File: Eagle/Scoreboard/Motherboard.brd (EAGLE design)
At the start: 59.4 x 80 mm, 24 parts

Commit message: Changed transistor type for score controller, changed number of terminals to 8. Motherboard still TBD
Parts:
- removed DISP_POWER: (no value), con-wago-500:W237-102
- added 12V, LED: (no value), con-wago-500:W237-102
- added R7: 470, resistor:0204/5
- added SG1: EB2505, buzzer:EB2505
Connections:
- new net 12V: 12V.1, 12V.2, C1.+, R7.2, REG.1, VCC.1
- net GND: now also LED.1; no longer DISP_POWER.1
- net N$7: now also LED.2, R7.1; no longer C1.+, REG.1, VCC.1
- net VCC: no longer DISP_POWER.2
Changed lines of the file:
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@@
 <attribute name="SPICEPREFIX" value="C" x="45.72" y="64.77" size="1.778" layer="27" rot="R270" display="off"/>
-</element>
-<element name="DISP_POWER" library="con-wago-500" library_urn="urn:adsk.eagle:library:195" package="W237-102" package3d_urn="urn:adsk.eagle:package:10688/1" value="" x="53.34" y="55.88" rot="R90">
-<attribute name="MF" value="" x="53.34" y="55.88" size="1.778" layer="27" rot="R90" display="off"/>
-<attribute name="MPN" value="237-102" x="53.34" y="55.88" size="1.778" layer="27" rot="R90" display="off"/>
-<attribute name="OC_FARNELL" value="unknown" x="53.34" y="55.88" size="1.778" layer="27" rot="R90" display="off"/>
-<attribute name="OC_NEWARK" value="70K9898" x="53.34" y="55.88" size="1.778" layer="27" rot="R90" display="off"/>
 </element>
 <element name="INFRA" library="con-wago-500" library_urn="urn:adsk.eagle:library:195" package="W237-103" package3d_urn="urn:adsk.eagle:package:10691/1" value="" x="53.34" y="12.7" rot="R90">
@@
 </element>
 <element name="R6" library="resistor" library_urn="urn:adsk.eagle:library:348" package="0204/5" package3d_urn="urn:adsk.eagle:package:25955/1" value="10k" x="30.48" y="15.24" rot="R180"/>
+<element name="12V" library="con-wago-500" library_urn="urn:adsk.eagle:library:195" package="W237-102" package3d_urn="urn:adsk.eagle:package:10688/1" value="" x="-7.62" y="8.89">
+<attribute name="MF" value="" x="-7.62" y="8.89" size="1.778" layer="27" display="off"/>
+<attribute name="MPN" value="237-102" x="-7.62" y="8.89" size="1.778" layer="27" display="off"/>
+<attribute name="OC_FARNELL" value="unknown" x="-7.62" y="8.89" size="1.778" layer="27" display="off"/>
+<attribute name="OC_NEWARK" value="70K9898" x="-7.62" y="8.89" size="1.778" layer="27" display="off"/>
+</element>
+<element name="R7" library="resistor" library_urn="urn:adsk.eagle:library:348" package="0204/5" package3d_urn="urn:adsk.eagle:package:25955/1" value="470" x="-8.89" y="-3.81"/>
+<element name="LED" library="con-wago-500" library_urn="urn:adsk.eagle:library:195" package="W237-102" package3d_urn="urn:adsk.eagle:package:10688/1" value="" x="-17.78" y="2.54">
+<attribute name="MF" value="" x="-17.78" y="2.54" size="1.778" layer="27" display="off"/>
+<attribute name="MPN" value="237-102" x="-17.78" y="2.54" size="1.778" layer="27" display="off"/>
+<attribute name="OC_FARNELL" value="unknown" x="-17.78" y="2.54" size="1.778" layer="27" display="off"/>
+<attribute name="OC_NEWARK" value="70K9898" x="-17.78" y="2.54" size="1.778" layer="27" display="off"/>
+</element>
+<element name="SG1" library="buzzer" library_urn="urn:adsk.eagle:library:113" package="EB2505" package3d_urn="urn:adsk.eagle:package:5275/1" value="EB2505" x="-35.56" y="6.35">
+<attribute name="MF" value="" x="-35.56" y="6.35" size="1.778" layer="27" display="off"/>
+<attribute name="MPN" value="" x="-35.56" y="6.35" size="1.778" layer="27" display="off"/>
+<attribute name="OC_FARNELL" value="unknown" x="-35.56" y="6.35" size="1.778" layer="27" display="off"/>
+<attribute name="OC_NEWARK" value="unknown" x="-35.56" y="6.35" size="1.778" layer="27" display="off"/>
+</element>
 </elements>
 <signals>
@@
 <contactref element="BTN_POW" pad="2"/>
 <contactref element="BLUETOOTH1" pad="2"/>
-<contactref element="DISP_POWER" pad="1"/>
 <contactref element="INFRA" pad="2"/>
 <contactref element="433MHZ" pad="1"/>
 <contactref element="ARDUINO_NANO1" pad="18"/>
 <contactref element="R6" pad="2"/>
+<contactref element="LED" pad="1"/>
 <wire x1="45.72" y1="63.754" x2="54.61" y2="68.54" width="0" layer="19" extent="1-1"/>
 <wire x1="39.37" y1="63.5" x2="45.72" y2="63.754" width="0" layer="19" extent="1-1"/>
@@
 <wire x1="40.68" y1="76.2" x2="35.56" y2="75.184" width="0" layer="19" extent="1-1"/>
 <wire x1="24.17" y1="76.2" x2="35.56" y2="75.184" width="0" layer="19" extent="1-1"/>
-<wire x1="54.61" y1="53.38" x2="45.72" y2="63.754" width="0" layer="19" extent="1-1"/>
-<wire x1="35.56" y1="35.56" x2="54.61" y2="53.38" width="0" layer="19" extent="1-1"/>
+<wire x1="35.56" y1="35.56" x2="39.37" y2="63.5" width="0" layer="19" extent="1-1"/>
 <wire x1="33.02" y1="35.56" x2="35.56" y2="35.56" width="0" layer="19" extent="1-1"/>
 <wire x1="38.1" y1="20.32" x2="35.56" y2="35.56" width="0" layer="19" extent="1-1"/>
@@
 <wire x1="54.63" y1="22.94" x2="38.1" y2="20.32" width="0" layer="19" extent="1-1"/>
 <wire x1="54.63" y1="12.7" x2="54.63" y2="22.94" width="0" layer="19" extent="1-1"/>
+<wire x1="-20.28" y1="1.27" x2="13.97" y2="12.7" width="0" layer="19" extent="1-1"/>
 </signal>
 <signal name="N$1">
@@
 <wire x1="34.25" y1="5.08" x2="27.94" y2="12.7" width="0" layer="19" extent="1-1"/>
 </signal>
-<signal name="N$7">
+<signal name="12V">
 <contactref element="VCC" pad="1"/>
 <contactref element="REG" pad="1"/>
 <contactref element="C1" pad="+"/>
+<contactref element="12V" pad="1"/>
+<contactref element="12V" pad="2"/>
+<contactref element="R7" pad="2"/>
 <wire x1="29.17" y1="76.2" x2="35.56" y2="77.216" width="0" layer="19" extent="1-1"/>
 <wire x1="39.37" y1="60.96" x2="35.56" y2="77.216" width="0" layer="19" extent="1-1"/>
+<wire x1="-5.12" y1="7.62" x2="39.37" y2="60.96" width="0" layer="19" extent="1-1"/>
+<wire x1="-10.12" y1="7.62" x2="-5.12" y2="7.62" width="0" layer="19" extent="1-1"/>
+<wire x1="-6.35" y1="-3.81" x2="-5.12" y2="7.62" width="0" layer="19" extent="1-1"/>
 </signal>
 <signal name="N$8">
@@
 <contactref element="BTN_POW" pad="1"/>
 <contactref element="BLUETOOTH1" pad="1"/>
-<contactref element="DISP_POWER" pad="2"/>
 <contactref element="INFRA" pad="3"/>
 <contactref element="433MHZ" pad="2"/>
 <wire x1="54.61" y1="63.54" x2="45.68" y2="76.2" width="0" layer="19" extent="1-1"/>
-<wire x1="54.61" y1="58.38" x2="54.61" y2="63.54" width="0" layer="19" extent="1-1"/>
-<wire x1="54.63" y1="27.94" x2="54.61" y2="58.38" width="0" layer="19" extent="1-1"/>
+<wire x1="54.63" y1="27.94" x2="54.61" y2="63.54" width="0" layer="19" extent="1-1"/>
 <wire x1="54.63" y1="17.7" x2="54.63" y2="27.94" width="0" layer="19" extent="1-1"/>
 <wire x1="33.02" y1="20.32" x2="54.63" y2="17.7" width="0" layer="19" extent="1-1"/>
@@
 <wire x1="5.08" y1="20.32" x2="54.63" y2="48.18" width="0" layer="19" extent="1-1"/>
 </signal>
+<signal name="N$7">
+<contactref element="R7" pad="1"/>
+<contactref element="LED" pad="2"/>
+<wire x1="-11.43" y1="-3.81" x2="-15.28" y2="1.27" width="0" layer="19" extent="1-1"/>
+</signal>
 </signals>

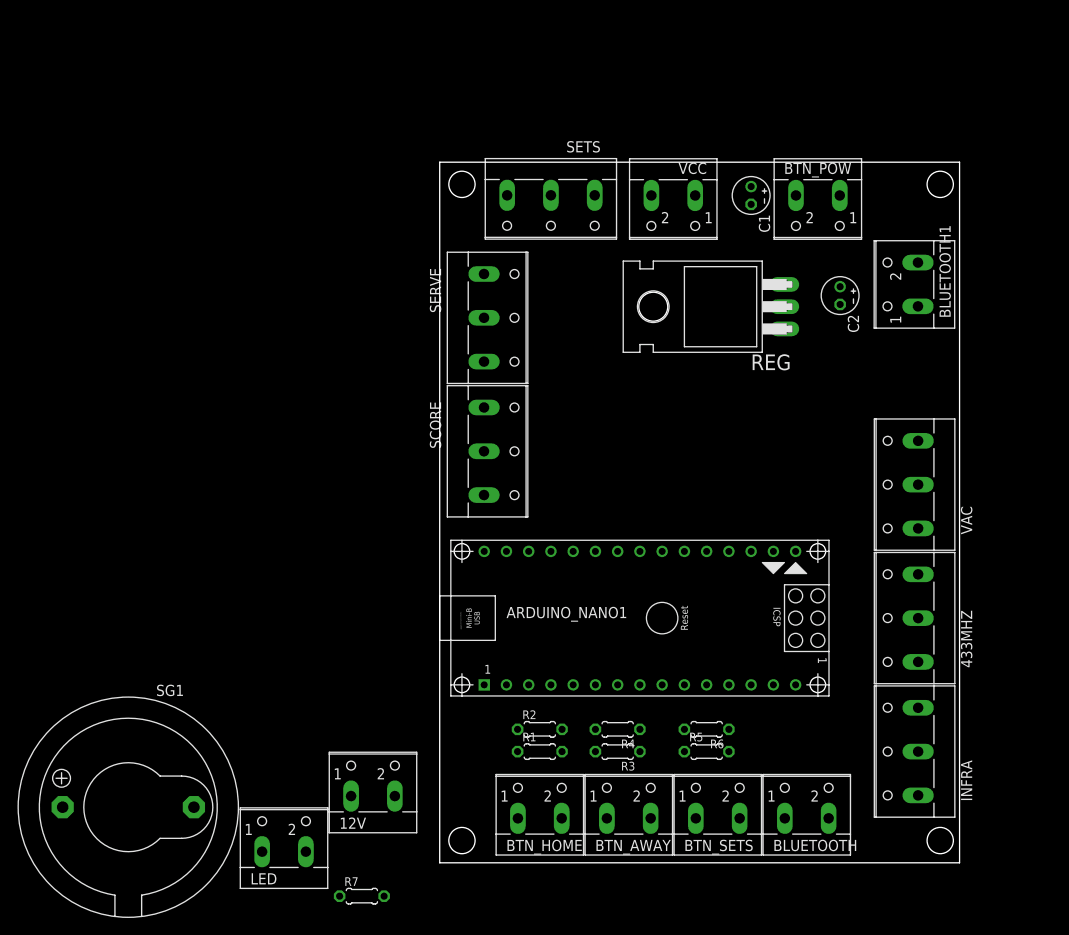
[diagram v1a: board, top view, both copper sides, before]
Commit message: Changed matherboard scheme and start designing PCB
Scheme was changed to make easier PCB design. Still need to finish VCC layer on TOP layer
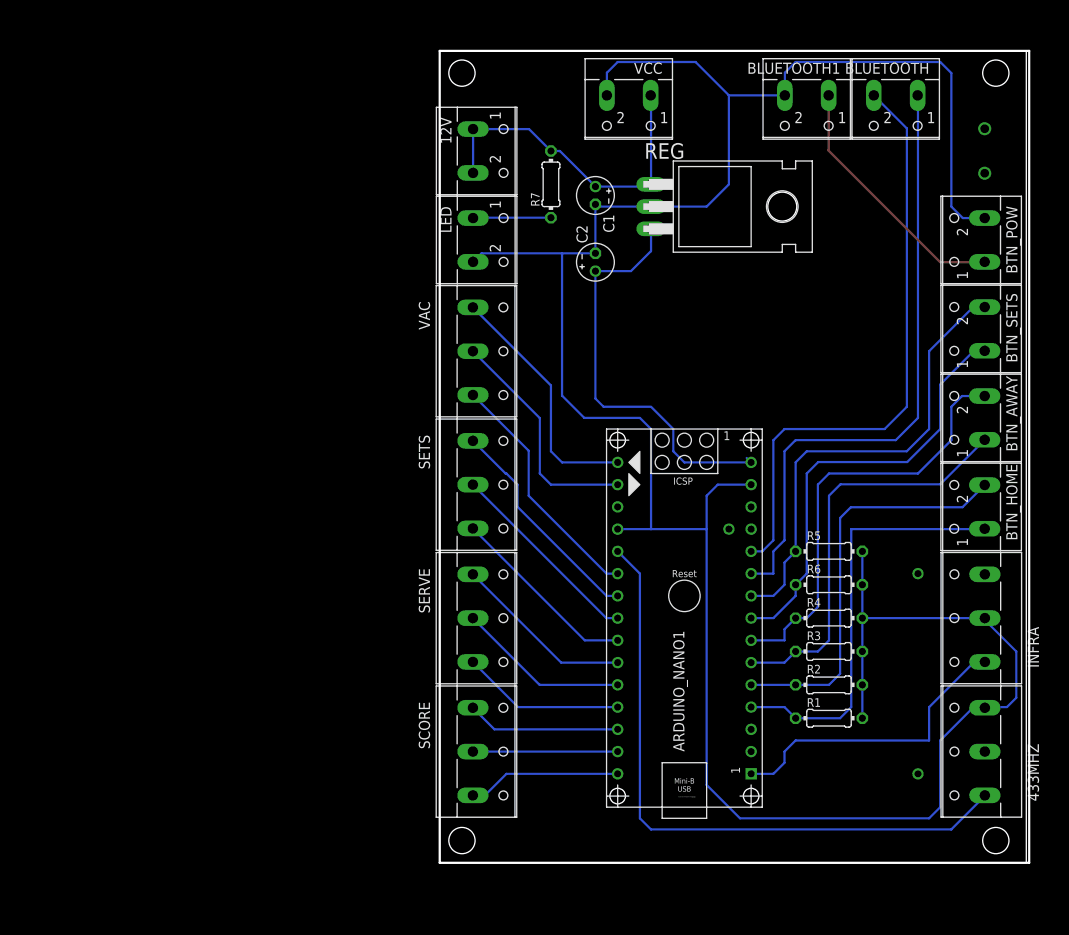
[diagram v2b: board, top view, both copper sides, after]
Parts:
- removed SG1: EB2505, buzzer:EB2505
- R1, R2, R3, R4, R5, R6, R7: device resistor:0204/5 -> resistor:0204/7
- moved R7 84.1 mm to (12.7, 77.5), turned to 90 degrees
- moved BLUETOOTH 80.7 mm to (52.1, 86.4), turned to 180 degrees
- moved 12V 73.5 mm to (5.08, 81.3), turned to 270 degrees
- moved LED 72.3 mm to (5.08, 71.1), turned to 270 degrees
- moved BTN_SETS 61.9 mm to (61.0, 61.0), turned to 90 degrees
- moved BTN_HOME 60.2 mm to (61.0, 40.6), turned to 90 degrees
- moved BTN_AWAY 59.4 mm to (61.0, 50.8), turned to 90 degrees
- moved VAC 50.6 mm to (5.08, 58.4), turned to 270 degrees
- moved SCORE 34.3 mm to (5.08, 12.7)
- moved SERVE 34.3 mm to (5.08, 27.9)
- moved R2 33.4 mm to (44.5, 20.3)
- moved R1 33.2 mm to (44.5, 16.5)
- moved SETS 32.7 mm to (5.08, 43.2), turned to 270 degrees
- moved C2 28.2 mm to (17.8, 68.6), turned to 90 degrees
- moved R4 27.3 mm to (44.5, 27.9), turned to 0 degrees
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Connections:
- net N$22 renamed VAC1
- net N$23 renamed VAC2
- removed net N$19: 433MHZ.3, ARDUINO_NANO1.20
- removed net N$20: ARDUINO_NANO1.21, INFRA.1
- removed net N$24: ARDUINO_NANO1.1, VAC.3
- removed net N$8: ARDUINO_NANO1.10, BLUETOOTH.2
- removed net N$9: ARDUINO_NANO1.11, BLUETOOTH.1
- new net 433MHZ: 433MHZ.1, ARDUINO_NANO1.20
- new net INFRA: ARDUINO_NANO1.1, INFRA.1
- new net RXD: ARDUINO_NANO1.11, BLUETOOTH.2
- new net TXD: ARDUINO_NANO1.10, BLUETOOTH.1
- new net VAC3: ARDUINO_NANO1.21, VAC.3
- net GND: now also 433MHZ.3, LED.2; no longer 433MHZ.1, ARDUINO_NANO1.18, LED.1
- net N$7: now also LED.1; no longer LED.2
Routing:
- net GND: track 0.00 -> 292.6 mm
- net 433MHZ: track 0.00 -> 73.1 mm
- net TXD: track 0.00 -> 70.7 mm
- net RXD: track 0.00 -> 68.4 mm
- net N$6: track 0.00 -> 53.0 mm
- net N$5: track 0.00 -> 51.0 mm
- net N$4: track 0.00 -> 49.4 mm
- net N$1: track 0.00 -> 48.1 mm
- net VIN: track 0.00 -> 47.4 mm
- net N$3: track 0.00 -> 46.9 mm
- net N$2: track 0.00 -> 46.5 mm
- net 12V: track 0.00 -> 39.6 mm
- net INFRA: track 0.00 -> 35.0 mm
- net VCC: track 0.00 -> 30.7 mm
- net VAC1: track 0.00 -> 28.3 mm
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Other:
- board size 59.4 x 80 mm -> 67.3 x 92.7 mm

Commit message: Finalized board for motherboard
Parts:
- removed 433MHZ, INFRA: (no value), con-wago-500:W237-103
- added 433MHZ_VC, INFRA_VC, SIGNAL_IN: (no value), con-wago-500:W237-102
- moved BLUETOOTH 36.7 mm to (61.0, 50.8), turned to 90 degrees
- moved BLUETOOTH1 31.8 mm to (61.0, 61.0), turned to 90 degrees
- moved BTN_HOME 20.3 mm to (61.0, 20.3)
- moved BTN_SETS 20.3 mm to (61.0, 40.6)
- moved BTN_AWAY 20.3 mm to (61.0, 30.5)
- moved R1 16.6 mm to (53.3, 30.5), turned to 90 degrees
- moved R2 12.0 mm to (50.8, 30.5), turned to 90 degrees
- moved 12V 8.13 mm to (11.4, 86.4), turned to 180 degrees
- moved R3 7.41 mm to (48.3, 30.5), turned to 90 degrees
- moved R5 6.35 mm to (40.6, 30.5), turned to 90 degrees
- moved R7 5.08 mm to (7.75, 78.6), turned to 0 degrees
- moved R4 2.84 mm to (45.7, 30.5), turned to 90 degrees
- moved R6 1.80 mm to (43.2, 30.5), turned to 90 degrees
- moved C1 1.27 mm to (17.8, 77.5)
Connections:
- net N$10 renamed SCORE_3
- net N$11 renamed SCORE_2
- net N$12 renamed SCORE_1
- net N$13 renamed SERVE_3
- net N$14 renamed SERVE_2
- net N$15 renamed SERVE_1
- net N$16 renamed SETS_3
- net N$17 renamed SETS_2
- net N$18 renamed SETS_1
- net VIN renamed VIN_9V
- removed net VAC2: ARDUINO_NANO1.17, VAC.2
- new net RESET: ARDUINO_NANO1.18, VAC.2
- net 433MHZ: now also SIGNAL_IN.1; no longer 433MHZ.1
- net GND: now also 433MHZ_VC.1, INFRA_VC.2; no longer 433MHZ.3, INFRA.2
- net INFRA: now also SIGNAL_IN.2; no longer INFRA.1
- net VCC: now also 433MHZ_VC.2, INFRA_VC.1; no longer 433MHZ.2, INFRA.3
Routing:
- net VCC: track 30.7 -> 84.6 mm
- net GND: track 292.6 -> 239.6 mm
- net TXD: track 70.7 -> 33.7 mm
- net RXD: track 68.4 -> 36.3 mm
- net RESET: track 0.00 -> 29.1 mm
- net VAC2: track 26.6 -> 0.00 mm
- net N$4: track 49.4 -> 33.4 mm
- net N$5: track 51.0 -> 36.3 mm
- net N$3: track 46.9 -> 33.1 mm
- net N$6: track 53.0 -> 39.6 mm
- net N$1: track 48.1 -> 35.6 mm
- net N$2: track 46.5 -> 37.2 mm
- net INFRA: track 35.0 -> 27.7 mm
- net VIN_9V: track 47.4 -> 40.2 mm
- net N$7: track 8.96 -> 5.05 mm
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- added copper zone on layer 16, net GND
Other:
- outline, holes or cut-outs redrawn
- board text added: "v1.0"
